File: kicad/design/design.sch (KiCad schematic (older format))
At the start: 7 parts, among them J1 Conn_USB_PWR, J2 Conn_USB_HEATER, J3 Conn_Temp_Probe, Q1 Q_NJFET_GDS, U1 HUZZAH32

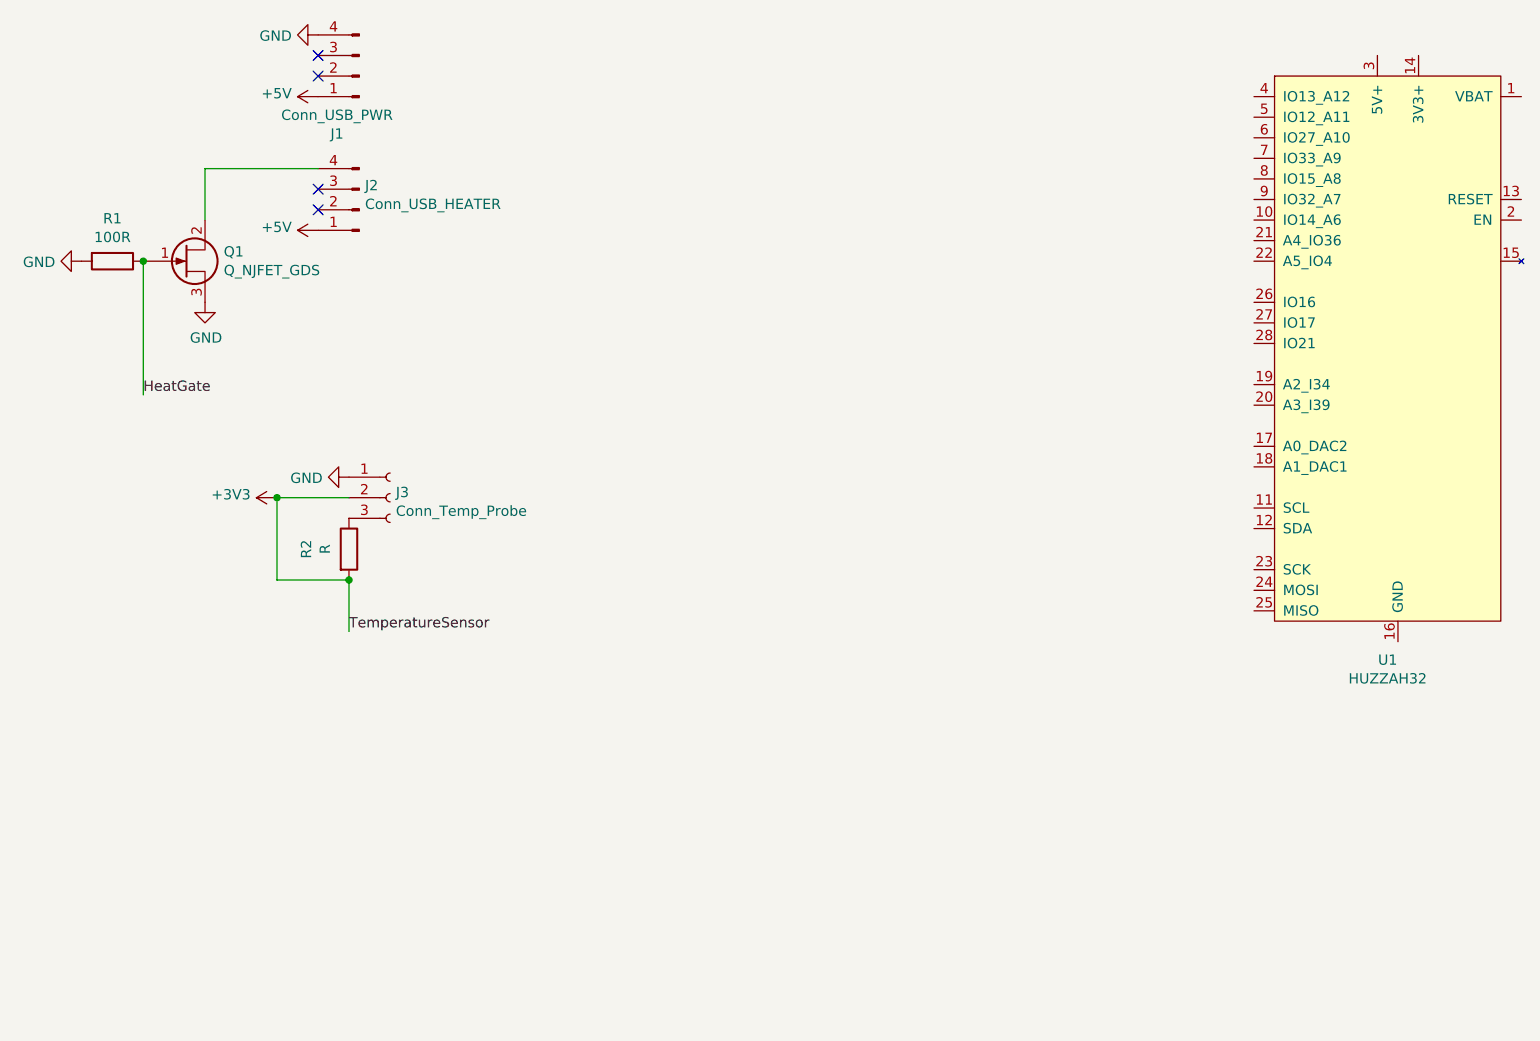
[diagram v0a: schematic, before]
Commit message: Added LED connector and some datasheets
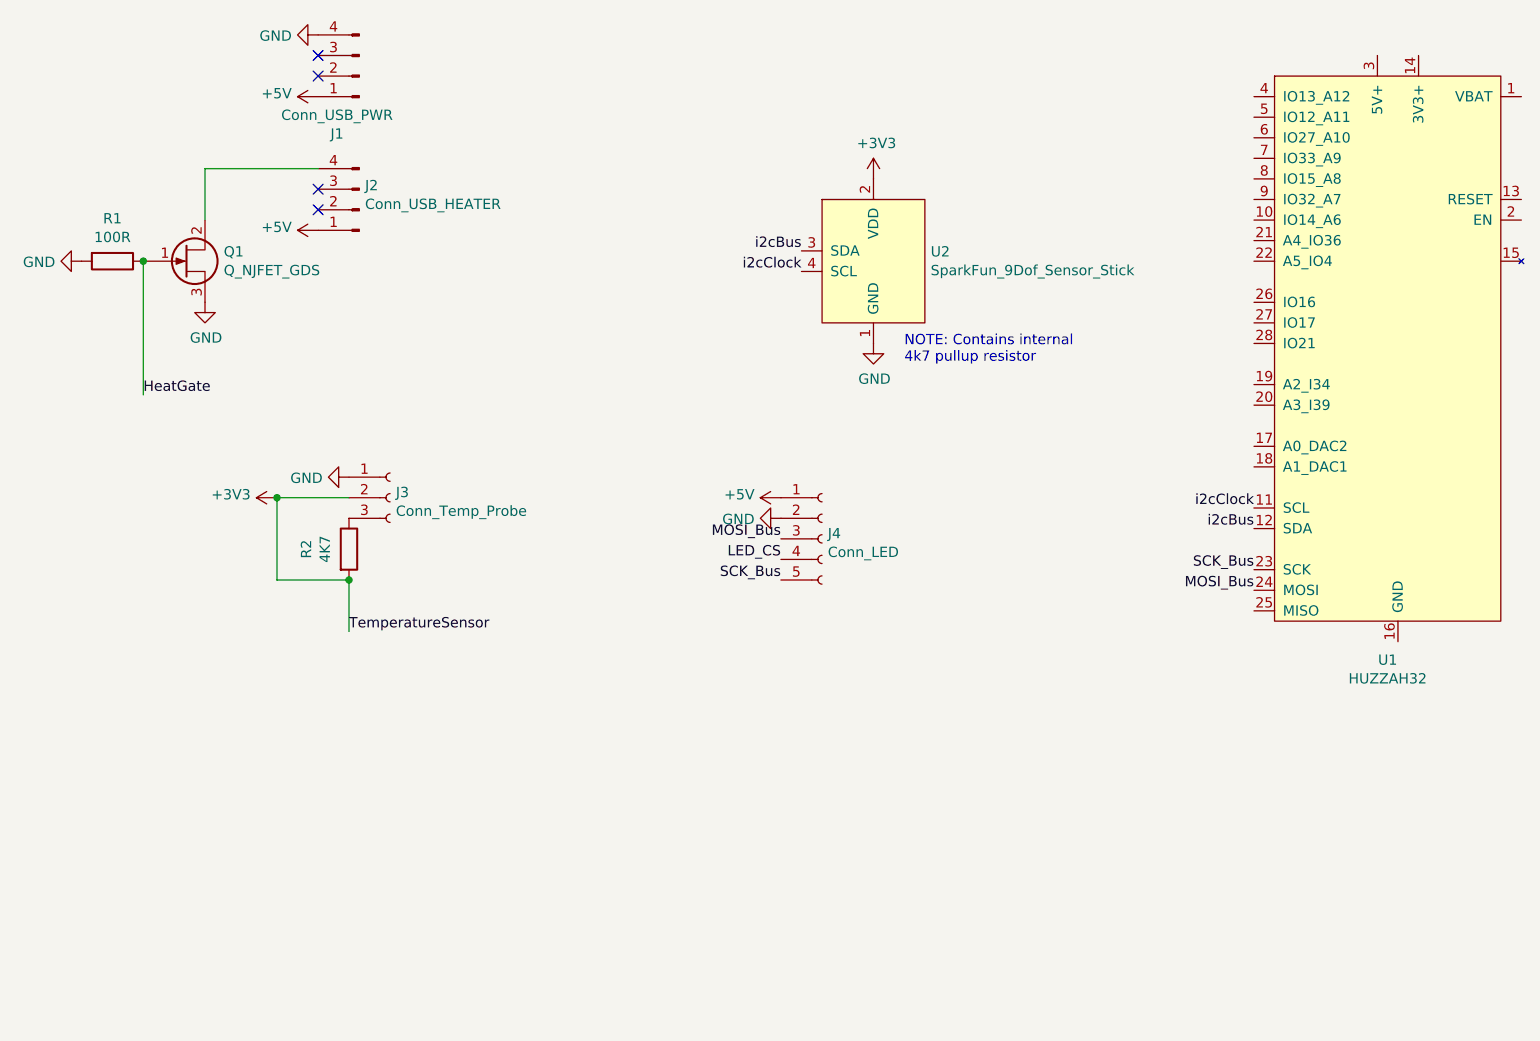
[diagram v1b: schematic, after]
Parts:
- added J4: Conn_LED, Connector_PinSocket_2.54mm:PinSocket_1x05_P2.54mm_Vertical, symbol Connector:Conn_01x05_Female
- added U2: SparkFun_9Dof_Sensor_Stick, Custom_Modules:SparkFun_9DoF_Sensor_Stick, symbol my_custom_library:SparkFun_9Dof_Sensor_Stick
- J1, J2: footprint (none) -> Connector_PinSocket_2.54mm:PinSocket_1x04_P2.54mm_Vertical
- J3: footprint (none) -> Connector_PinSocket_2.54mm:PinSocket_1x03_P2.54mm_Vertical
- R2: value R -> 4K7
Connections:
- net +3V3: now also U2.2 (VDD)
- net +5V: now also J4.1 (Pin_1)
- net GND: now also J4.2 (Pin_2), U2.1 (GND)
- net i2cClock: now reaches U1.11 (SCL)
- net i2cClock: now also U2.4 (SCL)
- net i2cBus: now reaches U1.12 (SDA)
- net i2cBus: now also U2.3 (SDA)
- net SCK_Bus: now reaches U1.23 (SCK)
- net SCK_Bus: now also J4.5 (Pin_5)
- net MOSI_Bus: now reaches U1.24 (MOSI)
- net MOSI_Bus: now also J4.3 (Pin_3)
- new net LED_CS: J4.4 (Pin_4)
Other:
- note added: "NOTE: Contains internal\n4k7 pullup resistor"
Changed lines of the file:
@@
 F 0 "J1" H 2758 1481 50  0000 C CNN
 F 1 "Conn_USB_PWR" H 2758 1390 50  0000 C CNN
-F 2 "" H 2650 1200 50  0001 C CNN
+F 2 "Connector_PinSocket_2.54mm:PinSocket_1x04_P2.54mm_Vertical" H 2650 1200 50  0001 C CNN
 F 3 "~" H 2650 1200 50  0001 C CNN
 	1    2650 1200
@@
 F 0 "J2" H 2622 1732 50  0000 R CNN
 F 1 "Conn_USB_HEATER" H 2622 1823 50  0000 R CNN
-F 2 "" H 2650 1850 50  0001 C CNN
+F 2 "Connector_PinSocket_2.54mm:PinSocket_1x04_P2.54mm_Vertical" H 2650 1850 50  0001 C CNN
 F 3 "~" H 2650 1850 50  0001 C CNN
 	1    2650 1850
@@
 F 0 "J3" H 2828 3276 50  0000 L CNN
 F 1 "Conn_Temp_Probe" H 2828 3185 50  0000 L CNN
-F 2 "" H 2800 3250 50  0001 C CNN
+F 2 "Connector_PinSocket_2.54mm:PinSocket_1x03_P2.54mm_Vertical" H 2800 3250 50  0001 C CNN
 F 3 "~" H 2800 3250 50  0001 C CNN
 	1    2800 3250
@@
 	0    1    1    0
 $EndComp
+Wire Wire Line
+	2250 3250 2600 3250
+$Comp
+L my_custom_library:SparkFun_9Dof_Sensor_Stick U2
+U 1 1 5D55D4E0
+P 5150 2150
+F 0 "U2" H 5428 2246 50  0000 L CNN
+F 1 "SparkFun_9Dof_Sensor_Stick" H 5428 2155 50  0000 L CNN
+F 2 "Custom_Modules:SparkFun_9DoF_Sensor_Stick" H 4850 2550 50  0001 C CNN
+F 3 "" H 4850 2550 50  0001 C CNN
+	1    5150 2150
+	1    0    0    -1
+$EndComp
+Wire Wire Line
+	2600 3650 2600 3900
 $Comp
 L Device:R R2
@@
 P 2600 3500
 F 0 "R2" V 2393 3500 50  0000 C CNN
-F 1 "R" V 2484 3500 50  0000 C CNN
+F 1 "4K7" V 2484 3500 50  0000 C CNN
 F 2 "" V 2530 3500 50  0001 C CNN
 F 3 "~" H 2600 3500 50  0001 C CNN
@@
 	1    0    0    -1
 $EndComp
-Wire Wire Line
-	2250 3250 2600 3250
-Wire Wire Line
-	2250 3250 2250 3650
+Connection ~ 2600 3650
 Wire Wire Line
 	2250 3650 2600 3650
 Connection ~ 2250 3250
 Wire Wire Line
-	2600 3650 2600 3900
-Connection ~ 2600 3650
+	2250 3250 2250 3650
 Text Label 2600 3900 0    50   ~ 0
 TemperatureSensor
+$Comp
+L power:+3V3 #PWR0101
+U 1 1 5D563AE9
+P 5150 1700
+F 0 "#PWR0101" H 5150 1550 50  0001 C CNN
+F 1 "+3V3" H 5165 1873 50  0000 C CNN
+F 2 "" H 5150 1700 50  0001 C CNN
+F 3 "" H 5150 1700 50  0001 C CNN
+	1    5150 1700
+	1    0    0    -1
+$EndComp
+$Comp
+L power:GND #PWR0102
+U 1 1 5D5641C9
+P 5150 2500
+F 0 "#PWR0102" H 5150 2250 50  0001 C CNN
+F 1 "GND" H 5155 2327 50  0000 C CNN
+F 2 "" H 5150 2500 50  0001 C CNN
+F 3 "" H 5150 2500 50  0001 C CNN
+	1    5150 2500
+	1    0    0    -1
+$EndComp
+Text Label 4800 2050 2    50   ~ 0
+i2cBus
+Text Label 7000 3400 2    50   ~ 0
+i2cBus
+Text Label 4800 2150 2    50   ~ 0
+i2cClock
+Text Label 7000 3300 2    50   ~ 0
+i2cClock
+Text Notes 5300 2600 0    50   ~ 0
+NOTE: Contains internal\n4k7 pullup resistor
+$Comp
+L Connector:Conn_01x05_Female J4
+U 1 1 5D568BF1
+P 4900 3450
+F 0 "J4" H 4928 3476 50  0000 L CNN
+F 1 "Conn_LED" H 4928 3385 50  0000 L CNN
+F 2 "Connector_PinSocket_2.54mm:PinSocket_1x05_P2.54mm_Vertical" H 4900 3450 50  0001 C CNN
+F 3 "~" H 4900 3450 50  0001 C CNN
+	1    4900 3450
+	1    0    0    -1
+$EndComp
+$Comp
+L power:+5V #PWR0103
+U 1 1 5D569E77
+P 4700 3250
+F 0 "#PWR0103" H 4700 3100 50  0001 C CNN
+F 1 "+5V" V 4715 3378 50  0000 L CNN
+F 2 "" H 4700 3250 50  0001 C CNN
+F 3 "" H 4700 3250 50  0001 C CNN
+	1    4700 3250
+	0    -1   -1   0
+$EndComp
+$Comp
+L power:GND #PWR0104
+U 1 1 5D56A9E5
+P 4700 3350
+F 0 "#PWR0104" H 4700 3100 50  0001 C CNN
+F 1 "GND" V 4705 3222 50  0000 R CNN
+F 2 "" H 4700 3350 50  0001 C CNN
+F 3 "" H 4700 3350 50  0001 C CNN
+	1    4700 3350
+	0    1    1    0
+$EndComp
+Text Label 4700 3450 2    50   ~ 0
+MOSI_Bus
+Text Label 4700 3650 2    50   ~ 0
+SCK_Bus
+Text Label 7000 3700 2    50   ~ 0
+MOSI_Bus
+Text Label 7000 3600 2    50   ~ 0
+SCK_Bus
+Text Label 4700 3550 2    50   ~ 0
+LED_CS
 $EndSCHEMATC

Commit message: did some stuff
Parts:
- added J5: Conn_Shutter, symbol Connector:Conn_01x03_Female
- added R3, R4: R, symbol Device:R
- added U3: ILD74, symbol Isolator:ILD74
- U1: symbol my_custom_library:HUZZAH32 -> design-rescue:HUZZAH32-my_custom_library
- U2: symbol my_custom_library:SparkFun_9Dof_Sensor_Stick -> design-rescue:SparkFun_9Dof_Sensor_Stick-my_custom_library
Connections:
- net GND: now also U3.2, U3.3
- new net: R3.1, U3.1
- new net: R4.1, U3.4
- new net CameraFocus: J5.2 (Pin_2), U3.7
- new net CameraGND: J5.1 (Pin_1), U3.5, U3.8
- new net CameraShutter: J5.3 (Pin_3), U3.6
- new net FocusSignal: R3.2
- new net ShutterSignal: R4.2
- no-connect marks 4 -> 5
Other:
- note added: "Note:\n1. Assume dual channel DIP8 Optocoupler\n2. Optocoupler yet to be chosen\n3. Resistor choice depends on max current of\n optocoupler IR LED."
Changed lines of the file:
@@
 EESchema Schematic File Version 4
-EELAYER 30 0
+LIBS:design-cache
+EELAYER 29 0
 EELAYER END
 $Descr A4 11693 8268
@@
 $EndDescr
 $Comp
-L my_custom_library:HUZZAH32 U1
+L design-rescue:HUZZAH32-my_custom_library U1
 U 1 1 5D523388
 P 7700 2650
@@
 	2250 3250 2600 3250
 $Comp
-L my_custom_library:SparkFun_9Dof_Sensor_Stick U2
+L design-rescue:SparkFun_9Dof_Sensor_Stick-my_custom_library U2
 U 1 1 5D55D4E0
 P 5150 2150
@@
 Text Label 4700 3550 2    50   ~ 0
 LED_CS
+$Comp
+L Connector:Conn_01x03_Female J5
+U 1 1 5D5372C8
+P 5750 4800
+F 0 "J5" H 5778 4826 50  0000 L CNN
+F 1 "Conn_Shutter" H 5778 4735 50  0000 L CNN
+F 2 "" H 5750 4800 50  0001 C CNN
+F 3 "~" H 5750 4800 50  0001 C CNN
+	1    5750 4800
+	1    0    0    -1
+$EndComp
+$Comp
+L Isolator:ILD74 U3
+U 1 1 5D53AFDD
+P 3650 4600
+F 0 "U3" H 3650 4925 50  0000 C CNN
+F 1 "ILD74" H 3650 4834 50  0000 C CNN
+F 2 "" H 3450 4400 50  0001 L CIN
+F 3 "https://www.vishay.com/docs/83640/ild74.pdf" H 3650 4600 50  0001 L CNN
+	1    3650 4600
+	1    0    0    -1
+$EndComp
+$Comp
+L Isolator:ILD74 U3
+U 2 1 5D53FAAC
+P 3650 5200
+F 0 "U3" H 3650 5525 50  0000 C CNN
+F 1 "ILD74" H 3650 5434 50  0000 C CNN
+F 2 "" H 3450 5000 50  0001 L CIN
+F 3 "https://www.vishay.com/docs/83640/ild74.pdf" H 3650 5200 50  0001 L CNN
+	2    3650 5200
+	1    0    0    -1
+$EndComp
+$Comp
+L Device:R R3
+U 1 1 5D541297
+P 3200 4500
+F 0 "R3" V 2993 4500 50  0000 C CNN
+F 1 "R" V 3084 4500 50  0000 C CNN
+F 2 "" V 3130 4500 50  0001 C CNN
+F 3 "~" H 3200 4500 50  0001 C CNN
+	1    3200 4500
+	0    1    1    0
+$EndComp
+$Comp
+L Device:R R4
+U 1 1 5D541B6C
+P 3200 5100
+F 0 "R4" V 2993 5100 50  0000 C CNN
+F 1 "R" V 3084 5100 50  0000 C CNN
+F 2 "" V 3130 5100 50  0001 C CNN
+F 3 "~" H 3200 5100 50  0001 C CNN
+	1    3200 5100
+	0    1    1    0
+$EndComp
+Text Label 3050 4500 2    50   ~ 0
+FocusSignal
+Text Label 3050 5100 2    50   ~ 0
+ShutterSignal
+$Comp
+L power:GND #PWR08
+U 1 1 5D542D11
+P 3350 4700
+F 0 "#PWR08" H 3350 4450 50  0001 C CNN
+F 1 "GND" V 3355 4572 50  0000 R CNN
+F 2 "" H 3350 4700 50  0001 C CNN
+F 3 "" H 3350 4700 50  0001 C CNN
+	1    3350 4700
+	0    1    1    0
+$EndComp
+$Comp
+L power:GND #PWR09
+U 1 1 5D5433E6
+P 3350 5300
+F 0 "#PWR09" H 3350 5050 50  0001 C CNN
+F 1 "GND" V 3355 5172 50  0000 R CNN
+F 2 "" H 3350 5300 50  0001 C CNN
+F 3 "" H 3350 5300 50  0001 C CNN
+	1    3350 5300
+	0    1    1    0
+$EndComp
+Text Label 5550 4700 2    50   ~ 0
+CameraGND
+Text Label 3950 4700 0    50   ~ 0
+CameraGND
+Text Label 3950 5300 0    50   ~ 0
+CameraGND
+Text Label 5550 4800 2    50   ~ 0
+CameraFocus
+Text Label 3950 4500 0    50   ~ 0
+CameraFocus
+Text Label 5550 4900 2    50   ~ 0
+CameraShutter
+Text Label 3950 5100 0    50   ~ 0
+CameraShutter
+Text Notes 2650 5800 0    50   ~ 0
+Note:\n1. Assume dual channel DIP8 Optocoupler\n2. Optocoupler yet to be chosen\n3. Resistor choice depends on max current of\n   optocoupler IR LED.
+NoConn ~ 7000 1400
 $EndSCHEMATC
